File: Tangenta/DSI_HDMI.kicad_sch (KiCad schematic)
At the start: 45 parts, among them J9 HDMI_19PIN_043, Q3 BSS138, Q4 BSS138, U15 LT8912B

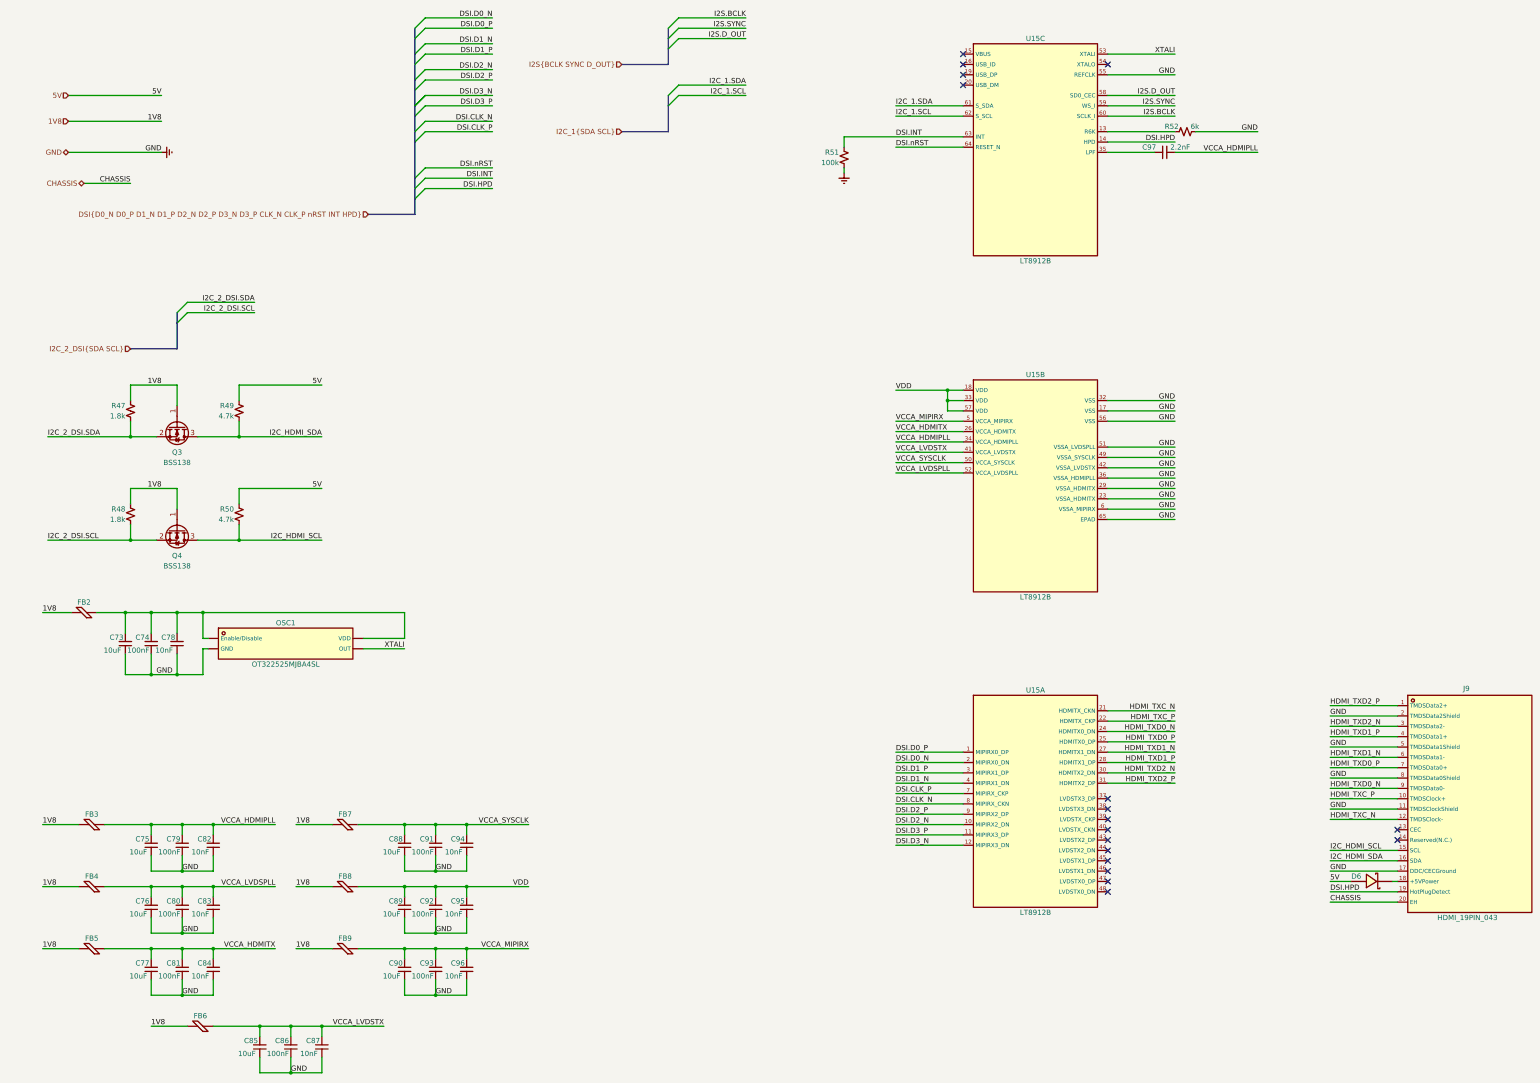
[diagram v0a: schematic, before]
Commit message: Reverting to the original design.
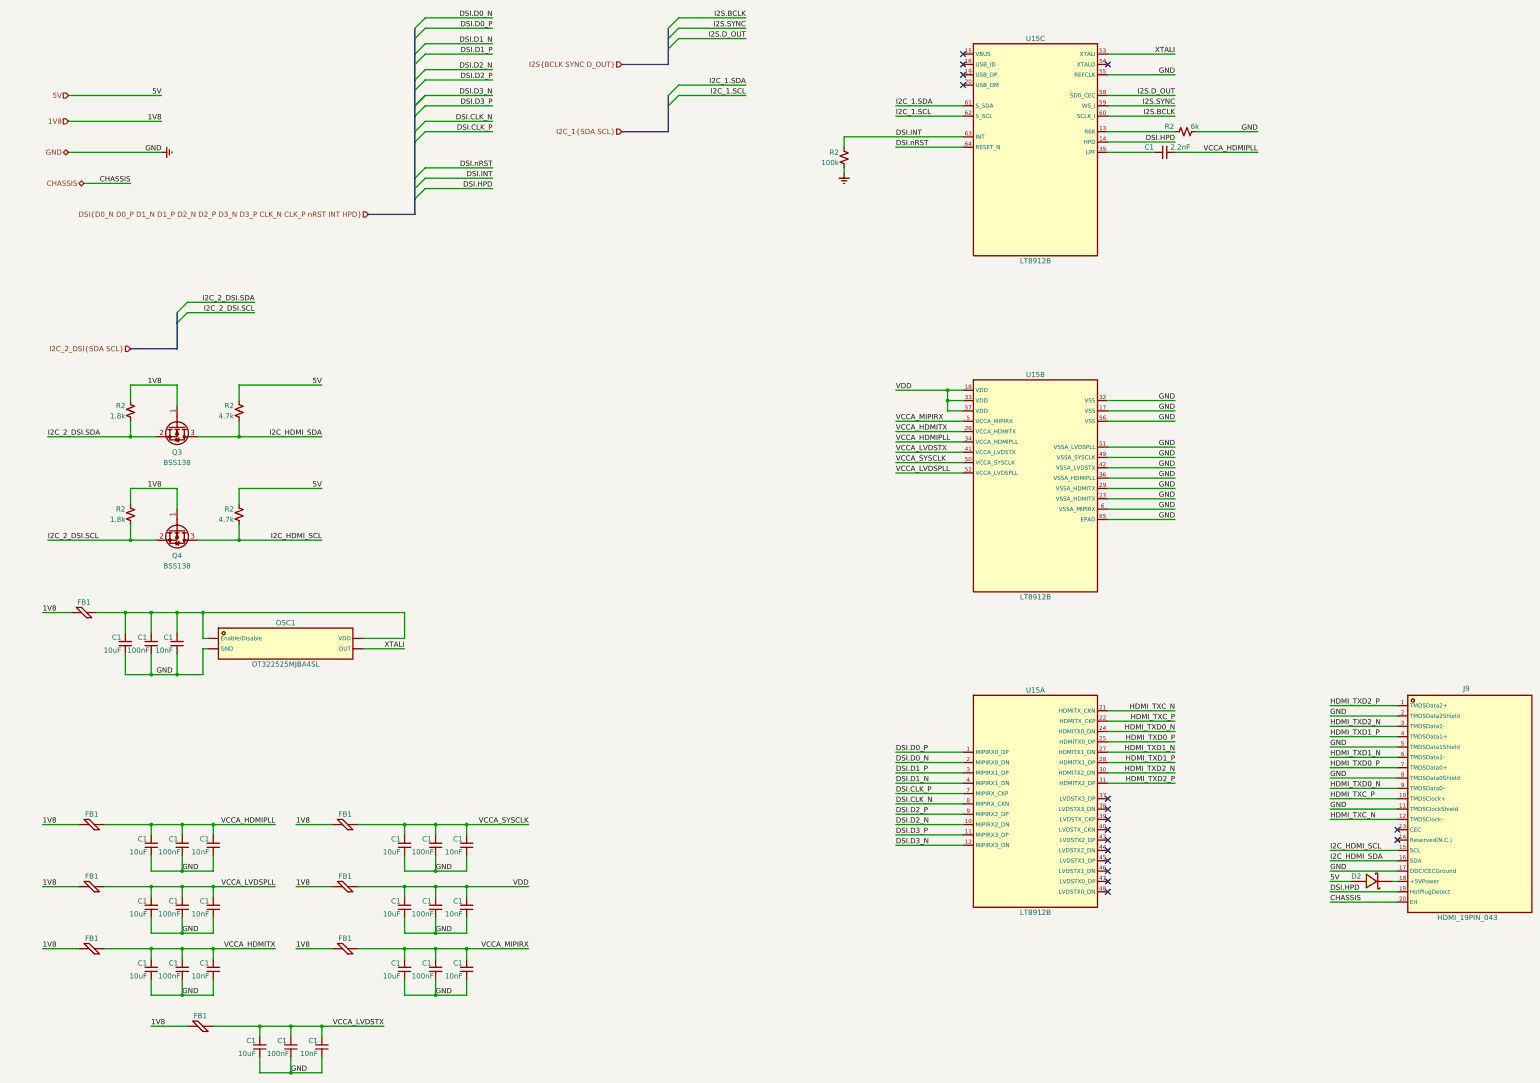
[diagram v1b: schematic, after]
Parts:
- C1: renamed from C97; symbol Device:C_Small -> CholaSymbolsPrjLib:C_Small
- C1: renamed from C77; symbol Device:C_Small -> CholaSymbolsPrjLib:C_Small
- C1: renamed from C96; symbol Device:C_Small -> CholaSymbolsPrjLib:C_Small
- C1: renamed from C84; symbol Device:C_Small -> CholaSymbolsPrjLib:C_Small
- C1: renamed from C90; symbol Device:C_Small -> CholaSymbolsPrjLib:C_Small
- C1: renamed from C92; symbol Device:C_Small -> CholaSymbolsPrjLib:C_Small
- C1: renamed from C91; symbol Device:C_Small -> CholaSymbolsPrjLib:C_Small
- C1: renamed from C81; symbol Device:C_Small -> CholaSymbolsPrjLib:C_Small
- C1: renamed from C78; symbol Device:C_Small -> CholaSymbolsPrjLib:C_Small
- C1: renamed from C73; symbol Device:C_Small -> CholaSymbolsPrjLib:C_Small
- C1: renamed from C76; symbol Device:C_Small -> CholaSymbolsPrjLib:C_Small
- C1: renamed from C85; symbol Device:C_Small -> CholaSymbolsPrjLib:C_Small
- C1: renamed from C74; symbol Device:C_Small -> CholaSymbolsPrjLib:C_Small
- C1: renamed from C94; symbol Device:C_Small -> CholaSymbolsPrjLib:C_Small
- C1: renamed from C89; symbol Device:C_Small -> CholaSymbolsPrjLib:C_Small
- C1: renamed from C95; symbol Device:C_Small -> CholaSymbolsPrjLib:C_Small
- C1: renamed from C75; symbol Device:C_Small -> CholaSymbolsPrjLib:C_Small
- C1: renamed from C80; symbol Device:C_Small -> CholaSymbolsPrjLib:C_Small
- C1: renamed from C93; symbol Device:C_Small -> CholaSymbolsPrjLib:C_Small
- C1: renamed from C87; symbol Device:C_Small -> CholaSymbolsPrjLib:C_Small
- C1: renamed from C88; symbol Device:C_Small -> CholaSymbolsPrjLib:C_Small
- C1: renamed from C83; symbol Device:C_Small -> CholaSymbolsPrjLib:C_Small
- C1: renamed from C86; symbol Device:C_Small -> CholaSymbolsPrjLib:C_Small
- C1: renamed from C79; symbol Device:C_Small -> CholaSymbolsPrjLib:C_Small
- C1: renamed from C82; symbol Device:C_Small -> CholaSymbolsPrjLib:C_Small
- D2: renamed from D6; symbol B540C-13-F:B540C-13-F -> CholaSymbolsPrjLib:B540C-13-F
- FB1: renamed from FB8; symbol Ferrite_Bead_100:GZ2012D101TF -> CholaSymbolsPrjLib:GZ2012D101TF
- FB1: renamed from FB4; symbol Ferrite_Bead_100:GZ2012D101TF -> CholaSymbolsPrjLib:GZ2012D101TF
- FB1: renamed from FB9; symbol Ferrite_Bead_100:GZ2012D101TF -> CholaSymbolsPrjLib:GZ2012D101TF
- FB1: renamed from FB7; symbol Ferrite_Bead_100:GZ2012D101TF -> CholaSymbolsPrjLib:GZ2012D101TF
- FB1: renamed from FB2; symbol Ferrite_Bead_100:GZ2012D101TF -> CholaSymbolsPrjLib:GZ2012D101TF
- FB1: renamed from FB6; symbol Ferrite_Bead_100:GZ2012D101TF -> CholaSymbolsPrjLib:GZ2012D101TF
- FB1: renamed from FB3; symbol Ferrite_Bead_100:GZ2012D101TF -> CholaSymbolsPrjLib:GZ2012D101TF
- FB1: renamed from FB5; symbol Ferrite_Bead_100:GZ2012D101TF -> CholaSymbolsPrjLib:GZ2012D101TF
- J9: symbol HDMI_CONNECTOR:HDMI_19PIN_043 -> CholaSymbolsPrjLib:HDMI_19PIN_043
- OSC1: symbol 25MHZ_OSCILLATOR:OT322525MJBA4SL -> CholaSymbolsPrjLib:OT322525MJBA4SL
- Q3, Q4: symbol Transistor_FET:BSS138 -> CholaSymbolsPrjLib:BSS138
- R2: renamed from R50; symbol Device:R_Small_US -> CholaSymbolsPrjLib:R_Small_US
- R2: renamed from R48; symbol Device:R_Small_US -> CholaSymbolsPrjLib:R_Small_US
- R2: renamed from R51; symbol Device:R_Small_US -> CholaSymbolsPrjLib:R_Small_US
- R2: renamed from R47; symbol Device:R_Small_US -> CholaSymbolsPrjLib:R_Small_US
- R2: renamed from R52; symbol Device:R_Small_US -> CholaSymbolsPrjLib:R_Small_US
- R2: renamed from R49; symbol Device:R_Small_US -> CholaSymbolsPrjLib:R_Small_US
- U15: symbol LT8912B:LT8912B -> CholaSymbolsPrjLib:LT8912B

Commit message: initialize branch
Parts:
- renumbered C1 to C73, C1 to C74, C1 to C75, C1 to C76, C1 to C77, C1 to C78, C1 to C79, C1 to C80, C1 to C81, C1 to C82, C1 to C83, C1 to C84, C1 to C85, C1 to C86, C1 to C87, C1 to C88, C1 to C89, C1 to C90, C1 to C91, C1 to C92, C1 to C93, C1 to C94, C1 to C95, C1 to C96, C1 to C97, D2 to D6, FB1 to FB2, FB1 to FB3, FB1 to FB4, FB1 to FB5, FB1 to FB6, FB1 to FB7, FB1 to FB8, FB1 to FB9, R2 to R47, R2 to R48, R2 to R49, R2 to R50, R2 to R51, R2 to R52

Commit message: U15-A,B,C,J9,OSC1
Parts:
- J9: footprint HDMI_CONNECTOR:HDMI_CONNECTOR -> CholaFootprintsPrjLib:HDMI_CONNECTOR
- OSC1: footprint 25MHZ_OSCILLATOR:25MHZ_OSCILLATOR -> CholaFootprintsPrjLib:25MHZ_OSCILLATOR
- U15: footprint LT8912B:LT8912B -> CholaFootprintsPrjLib:LT8912B
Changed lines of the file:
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@@
     )
   )
-  (symbol (lib_id "CholaSymbolsPrjLib:LT8912B") (at 264.16 228.6 0) (unit 1)
+  (symbol (lib_name "LT8912B_1") (lib_id "CholaSymbolsPrjLib:LT8912B") (at 264.16 228.6 0) (unit 1)
     (in_bom yes) (on_board yes) (dnp no)
     (property "Reference" "U15" (at 264.16 185.42 0)
@@
       (effects (font (size 1.27 1.27)))
     )
-    (property "Footprint" "LT8912B:LT8912B" (at 257.81 247.65 0)
+    (property "Footprint" "CholaFootprintsPrjLib:LT8912B" (at 257.81 247.65 0)
       (effects (font (size 1.27 1.27) italic) hide)
     )
@@
     )
   )
-  (symbol (lib_id "CholaSymbolsPrjLib:LT8912B") (at 264.16 151.13 0) (unit 2)
+  (symbol (lib_name "LT8912B_2") (lib_id "CholaSymbolsPrjLib:LT8912B") (at 264.16 151.13 0) (unit 2)
     (in_bom yes) (on_board yes) (dnp no)
     (property "Reference" "U15" (at 264.16 107.95 0)
@@
       (effects (font (size 1.27 1.27)))
     )
-    (property "Footprint" "LT8912B:LT8912B" (at 257.81 170.18 0)
+    (property "Footprint" "CholaFootprintsPrjLib:LT8912B" (at 257.81 170.18 0)
       (effects (font (size 1.27 1.27) italic) hide)
     )
@@
       (effects (font (size 1.27 1.27)) (justify left))
     )
-    (property "Footprint" "HDMI_CONNECTOR:HDMI_CONNECTOR" (at 372.11 246.38 0)
+    (property "Footprint" "CholaFootprintsPrjLib:HDMI_CONNECTOR" (at 372.11 246.38 0)
       (effects (font (size 1.27 1.27) italic) hide)
     )
@@
       (effects (font (size 1.27 1.27)))
     )
-    (property "Footprint" "LT8912B:LT8912B" (at 257.81 87.63 0)
+    (property "Footprint" "CholaFootprintsPrjLib:LT8912B" (at 257.81 87.63 0)
       (effects (font (size 1.27 1.27) italic) hide)
     )
@@
       (effects (font (size 1.27 1.27)))
     )
-    (property "Footprint" "25MHZ_OSCILLATOR:25MHZ_OSCILLATOR" (at 81.534 186.055 0)
+    (property "Footprint" "CholaFootprintsPrjLib:25MHZ_OSCILLATOR" (at 81.534 186.055 0)
       (effects (font (size 1.27 1.27) italic) hide)
     )

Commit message: FB5-FB13, D6
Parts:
- D6: footprint B540C-13-F:B540C-13-F -> CholaFootprintsPrjLib:B540C-13-F
- FB2, FB3, FB4, FB5, FB6, FB7, FB8, FB9: footprint Ferrite_Bead_100:Ferrite_Bead_100 -> CholaFootprintsPrjLib:Ferrite_Bead_100
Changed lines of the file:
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@@
     )
   )
-  (symbol (lib_id "CholaSymbolsPrjLib:GZ2012D101TF") (at 94.615 233.68 0) (unit 1)
+  (symbol (lib_name "GZ2012D101TF_7") (lib_id "CholaSymbolsPrjLib:GZ2012D101TF") (at 94.615 233.68 0) (unit 1)
     (in_bom yes) (on_board yes) (dnp no)
     (property "Reference" "FB8" (at 94.615 231.14 0)
@@
       (effects (font (size 1.27 1.27)) hide)
     )
-    (property "Footprint" "Ferrite_Bead_100:Ferrite_Bead_100" (at 107.188 243.713 0)
+    (property "Footprint" "CholaFootprintsPrjLib:Ferrite_Bead_100" (at 107.188 243.713 0)
       (effects (font (size 1.27 1.27) italic) hide)
     )
@@
       (effects (font (size 1.27 1.27)) (justify left) hide)
     )
-    (property "Footprint" "B540C-13-F:B540C-13-F" (at 346.583 220.853 0)
+    (property "Footprint" "CholaFootprintsPrjLib:B540C-13-F" (at 346.583 220.853 0)
       (effects (font (size 1.27 1.27) italic) hide)
     )
@@
     )
   )
-  (symbol (lib_id "CholaSymbolsPrjLib:GZ2012D101TF") (at 32.385 233.68 0) (unit 1)
+  (symbol (lib_name "GZ2012D101TF_3") (lib_id "CholaSymbolsPrjLib:GZ2012D101TF") (at 32.385 233.68 0) (unit 1)
     (in_bom yes) (on_board yes) (dnp no)
     (property "Reference" "FB4" (at 32.385 231.14 0)
@@
       (effects (font (size 1.27 1.27)) hide)
     )
-    (property "Footprint" "Ferrite_Bead_100:Ferrite_Bead_100" (at 44.958 243.713 0)
+    (property "Footprint" "CholaFootprintsPrjLib:Ferrite_Bead_100" (at 44.958 243.713 0)
       (effects (font (size 1.27 1.27) italic) hide)
     )
@@
       (effects (font (size 1.27 1.27)) hide)
     )
-    (property "Footprint" "Ferrite_Bead_100:Ferrite_Bead_100" (at 107.188 258.953 0)
+    (property "Footprint" "CholaFootprintsPrjLib:Ferrite_Bead_100" (at 107.188 258.953 0)
       (effects (font (size 1.27 1.27) italic) hide)
     )
@@
     )
   )
-  (symbol (lib_id "CholaSymbolsPrjLib:GZ2012D101TF") (at 94.615 218.44 0) (unit 1)
+  (symbol (lib_name "GZ2012D101TF_6") (lib_id "CholaSymbolsPrjLib:GZ2012D101TF") (at 94.615 218.44 0) (unit 1)
     (in_bom yes) (on_board yes) (dnp no)
     (property "Reference" "FB7" (at 94.615 215.9 0)
@@
       (effects (font (size 1.27 1.27)) hide)
     )
-    (property "Footprint" "Ferrite_Bead_100:Ferrite_Bead_100" (at 107.188 228.473 0)
+    (property "Footprint" "CholaFootprintsPrjLib:Ferrite_Bead_100" (at 107.188 228.473 0)
       (effects (font (size 1.27 1.27) italic) hide)
     )
@@
     )
   )
-  (symbol (lib_id "CholaSymbolsPrjLib:GZ2012D101TF") (at 30.48 166.37 0) (unit 1)
+  (symbol (lib_name "GZ2012D101TF_1") (lib_id "CholaSymbolsPrjLib:GZ2012D101TF") (at 30.48 166.37 0) (unit 1)
     (in_bom yes) (on_board yes) (dnp no)
     (property "Reference" "FB2" (at 30.48 163.83 0)
@@
       (effects (font (size 1.27 1.27)) hide)
     )
-    (property "Footprint" "Ferrite_Bead_100:Ferrite_Bead_100" (at 43.053 176.403 0)
+    (property "Footprint" "CholaFootprintsPrjLib:Ferrite_Bead_100" (at 43.053 176.403 0)
       (effects (font (size 1.27 1.27) italic) hide)
     )
@@
     )
   )
-  (symbol (lib_id "CholaSymbolsPrjLib:GZ2012D101TF") (at 59.055 267.97 0) (unit 1)
+  (symbol (lib_name "GZ2012D101TF_5") (lib_id "CholaSymbolsPrjLib:GZ2012D101TF") (at 59.055 267.97 0) (unit 1)
     (in_bom yes) (on_board yes) (dnp no)
     (property "Reference" "FB6" (at 59.055 265.43 0)
@@
       (effects (font (size 1.27 1.27)) hide)
     )
-    (property "Footprint" "Ferrite_Bead_100:Ferrite_Bead_100" (at 71.628 278.003 0)
+    (property "Footprint" "CholaFootprintsPrjLib:Ferrite_Bead_100" (at 71.628 278.003 0)
       (effects (font (size 1.27 1.27) italic) hide)
     )
@@
     )
   )
-  (symbol (lib_id "CholaSymbolsPrjLib:GZ2012D101TF") (at 32.385 218.44 0) (unit 1)
+  (symbol (lib_name "GZ2012D101TF_2") (lib_id "CholaSymbolsPrjLib:GZ2012D101TF") (at 32.385 218.44 0) (unit 1)
     (in_bom yes) (on_board yes) (dnp no)
     (property "Reference" "FB3" (at 32.385 215.9 0)
@@
       (effects (font (size 1.27 1.27)) hide)
     )
-    (property "Footprint" "Ferrite_Bead_100:Ferrite_Bead_100" (at 44.958 228.473 0)
+    (property "Footprint" "CholaFootprintsPrjLib:Ferrite_Bead_100" (at 44.958 228.473 0)
       (effects (font (size 1.27 1.27) italic) hide)
     )
@@
     )
   )
-  (symbol (lib_id "CholaSymbolsPrjLib:GZ2012D101TF") (at 32.385 248.92 0) (unit 1)
+  (symbol (lib_name "GZ2012D101TF_4") (lib_id "CholaSymbolsPrjLib:GZ2012D101TF") (at 32.385 248.92 0) (unit 1)
     (in_bom yes) (on_board yes) (dnp no)
     (property "Reference" "FB5" (at 32.385 246.38 0)
@@
       (effects (font (size 1.27 1.27)) hide)
     )
-    (property "Footprint" "Ferrite_Bead_100:Ferrite_Bead_100" (at 44.958 258.953 0)
-      (effects (font (size 1.27 1.27) italic) hide)
-    )
+    (property "Footprint" "CholaFootprintsPrjLib:Ferrite_Bead_100" (at 44.958 258.953 0)
+      (effects (font (size 1.27 1.27) italic) hide)
+    )
